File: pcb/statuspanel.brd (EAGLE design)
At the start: 57.1 x 66 mm, 5 parts

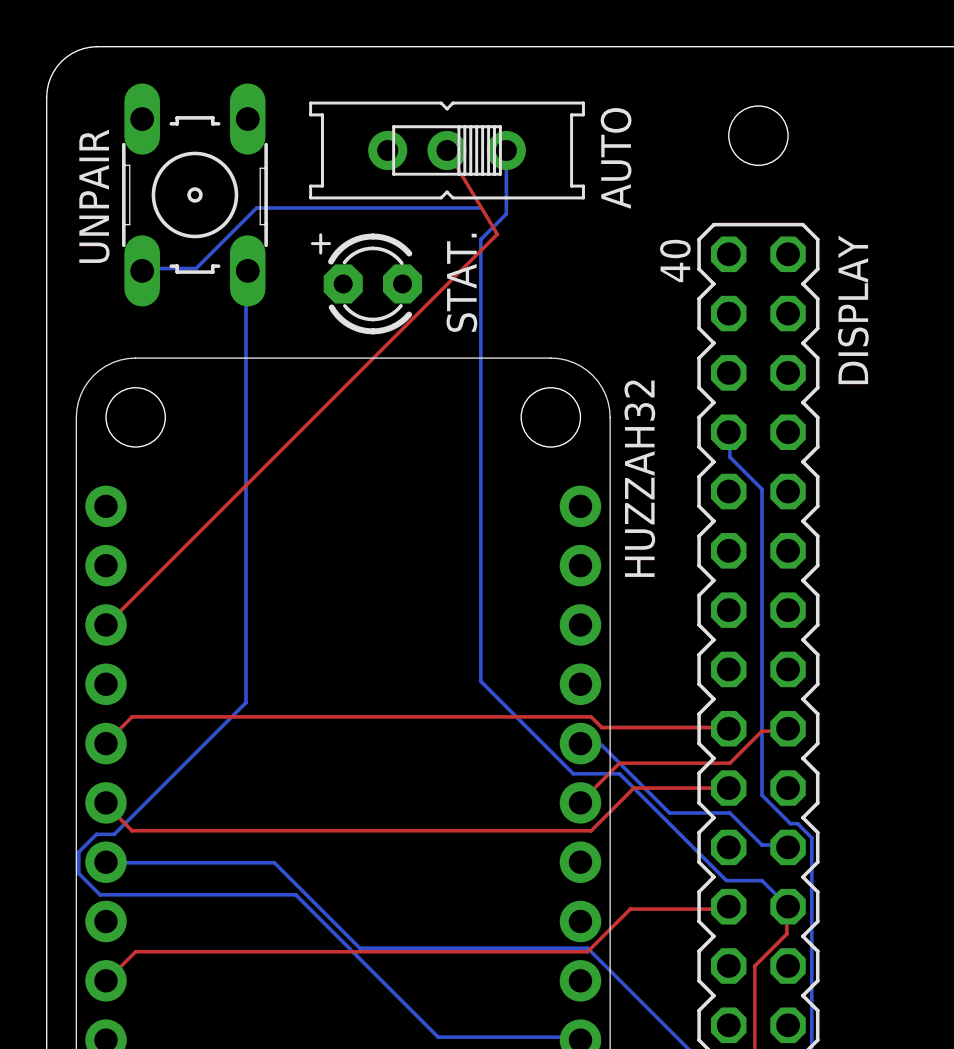
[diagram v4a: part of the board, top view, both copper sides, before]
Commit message: Connect up one leg of the LED
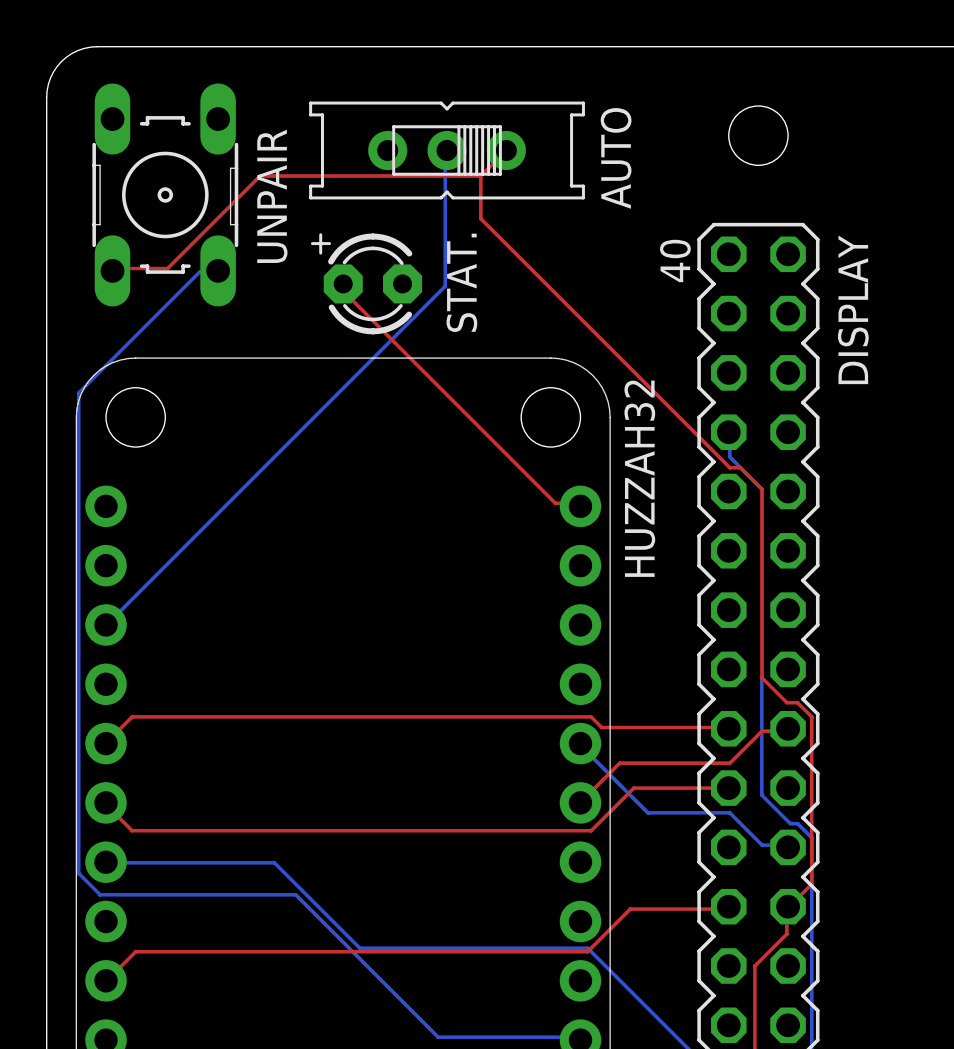
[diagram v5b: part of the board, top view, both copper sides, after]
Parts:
- moved UNPAIR 1.27 mm to (5.08, 59.7)
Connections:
- new net N$3: STAT..K
- new net STATUS: HUZZAH32.16, STAT..A
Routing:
- net STATUS: track 0.00 -> 14.4 mm
- net AUTO: track 27.9 -> 26.4 mm
- net 3V3: track 85.7 -> 86.9 mm
- net UNPAIR: track 53.8 -> 53.2 mm
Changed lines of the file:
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@@
 <attribute name="NAME" x="23.749" y="63.5" size="1.27" layer="25" font="vector" rot="R270"/>
 </element>
-<element name="UNPAIR" library="switch-omron" library_urn="urn:adsk.eagle:library:377" package="B3F-10XX" package3d_urn="urn:adsk.eagle:package:27496/1" value="" x="6.35" y="59.69" smashed="yes" rot="R90">
-<attribute name="MF" value="" x="6.35" y="59.69" size="1.778" layer="27" rot="R90" display="off"/>
-<attribute name="MPN" value="B3F-1000" x="6.35" y="59.69" size="1.778" layer="27" rot="R90" display="off"/>
-<attribute name="NAME" x="2.667" y="56.642" size="1.27" layer="25" ratio="10" rot="R90"/>
-<attribute name="OC_FARNELL" value="176432" x="6.35" y="59.69" size="1.778" layer="27" rot="R90" display="off"/>
-<attribute name="OC_NEWARK" value="36M3542" x="6.35" y="59.69" size="1.778" layer="27" rot="R90" display="off"/>
-<attribute name="POPULARITY" value="72" x="6.35" y="59.69" size="1.778" layer="27" rot="R90" display="off"/>
-<attribute name="VALUE" x="11.43" y="56.642" size="1.27" layer="27" ratio="10" rot="R90"/>
+<element name="UNPAIR" library="switch-omron" library_urn="urn:adsk.eagle:library:377" package="B3F-10XX" package3d_urn="urn:adsk.eagle:package:27496/1" value="" x="5.08" y="59.69" smashed="yes" rot="R90">
+<attribute name="MF" value="" x="5.08" y="59.69" size="1.778" layer="27" rot="R90" display="off"/>
+<attribute name="MPN" value="B3F-1000" x="5.08" y="59.69" size="1.778" layer="27" rot="R90" display="off"/>
+<attribute name="NAME" x="10.287" y="56.642" size="1.27" layer="25" ratio="10" rot="R90"/>
+<attribute name="OC_FARNELL" value="176432" x="5.08" y="59.69" size="1.778" layer="27" rot="R90" display="off"/>
+<attribute name="OC_NEWARK" value="36M3542" x="5.08" y="59.69" size="1.778" layer="27" rot="R90" display="off"/>
+<attribute name="POPULARITY" value="72" x="5.08" y="59.69" size="1.778" layer="27" rot="R90" display="off"/>
+<attribute name="VALUE" x="10.16" y="56.642" size="1.27" layer="27" ratio="10" rot="R90"/>
 </element>
 <element name="STAT." library="adafruit" library_urn="urn:adsk.eagle:library:420" package="LED3MM" package3d_urn="urn:adsk.eagle:package:6240537/1" value="" x="13.97" y="55.88" smashed="yes">
@@
 <wire x1="30.6324" y1="31.8516" x2="31.6992" y2="31.8516" width="0.1524" layer="16"/>
 <wire x1="29.2608" y1="33.2232" x2="30.6324" y2="31.8516" width="0.1524" layer="16"/>
-<wire x1="26.67" y1="33.2232" x2="29.2608" y2="33.2232" width="0.1524" layer="16"/>
-<wire x1="23.7744" y1="36.1188" x2="26.67" y2="33.2232" width="0.1524" layer="16"/>
-<wire x1="22.86" y1="36.1188" x2="23.7744" y2="36.1188" width="0.1524" layer="16"/>
+<wire x1="25.7556" y1="33.2232" x2="29.2608" y2="33.2232" width="0.1524" layer="16"/>
+<wire x1="22.86" y1="36.1188" x2="25.7556" y2="33.2232" width="0.1524" layer="16"/>
 <wire x1="31.6992" y1="31.8516" x2="31.75" y2="31.75" width="0.1524" layer="16"/>
 <wire x1="22.86" y1="36.1188" x2="22.86" y2="36.195" width="0.1524" layer="16"/>
@@
 <contactref element="AUTO" pad="O"/>
 <contactref element="UNPAIR" pad="1"/>
-<wire x1="6.4008" y1="56.5404" x2="4.1148" y2="56.5404" width="0.1524" layer="16"/>
-<wire x1="8.9916" y1="59.1312" x2="6.4008" y2="56.5404" width="0.1524" layer="16"/>
-<wire x1="18.5928" y1="59.1312" x2="8.9916" y2="59.1312" width="0.1524" layer="16"/>
-<wire x1="4.1148" y1="56.5404" x2="4.0894" y2="56.4388" width="0.1524" layer="16"/>
-<wire x1="19.685" y1="61.595" x2="19.685" y2="58.8772" width="0.1524" layer="16"/>
-<wire x1="19.685" y1="58.8772" x2="18.5928" y2="57.785" width="0.1524" layer="16"/>
+<wire x1="5.1816" y1="56.5404" x2="2.8956" y2="56.5404" width="0.1524" layer="1"/>
+<wire x1="9.144" y1="60.5028" x2="5.1816" y2="56.5404" width="0.1524" layer="1"/>
+<wire x1="18.5928" y1="60.5028" x2="9.144" y2="60.5028" width="0.1524" layer="1"/>
+<wire x1="19.685" y1="61.595" x2="18.5928" y2="60.5028" width="0.1524" layer="1"/>
+<wire x1="2.8956" y1="56.5404" x2="2.8194" y2="56.4388" width="0.1524" layer="1"/>
 <wire x1="30.6324" y1="8.9916" x2="31.6992" y2="8.9916" width="0.1524" layer="1"/>
 <wire x1="29.2608" y1="10.3632" x2="29.4132" y2="10.2108" width="0.1524" layer="1"/>
@@
 <wire x1="29.4132" y1="10.2108" x2="30.3276" y2="11.1252" width="0.1524" layer="1"/>
 <wire x1="31.6992" y1="29.1084" x2="31.75" y2="29.21" width="0.1524" layer="1"/>
-<wire x1="18.5928" y1="38.862" x2="18.5928" y2="57.785" width="0.1524" layer="16"/>
-<wire x1="22.5552" y1="34.8996" x2="18.5928" y2="38.862" width="0.1524" layer="16"/>
-<wire x1="24.5364" y1="34.8996" x2="22.5552" y2="34.8996" width="0.1524" layer="16"/>
-<wire x1="29.1084" y1="30.3276" x2="24.5364" y2="34.8996" width="0.1524" layer="16"/>
-<wire x1="30.6324" y1="30.3276" x2="29.1084" y2="30.3276" width="0.1524" layer="16"/>
-<wire x1="31.75" y1="29.21" x2="30.6324" y2="30.3276" width="0.1524" layer="16"/>
+<wire x1="18.5928" y1="58.674" x2="18.5928" y2="60.5028" width="0.1524" layer="1"/>
+<wire x1="29.2608" y1="48.006" x2="18.5928" y2="58.674" width="0.1524" layer="1"/>
+<wire x1="29.718" y1="48.006" x2="29.2608" y2="48.006" width="0.1524" layer="1"/>
+<wire x1="30.6324" y1="47.0916" x2="29.718" y2="48.006" width="0.1524" layer="1"/>
+<wire x1="30.6324" y1="39.0144" x2="30.6324" y2="47.0916" width="0.1524" layer="1"/>
+<wire x1="31.6992" y1="37.9476" x2="30.6324" y2="39.0144" width="0.1524" layer="1"/>
+<wire x1="32.1564" y1="37.9476" x2="31.6992" y2="37.9476" width="0.1524" layer="1"/>
+<wire x1="32.766" y1="37.338" x2="32.1564" y2="37.9476" width="0.1524" layer="1"/>
+<wire x1="32.766" y1="30.1752" x2="32.766" y2="37.338" width="0.1524" layer="1"/>
+<wire x1="31.8516" y1="29.2608" x2="32.766" y2="30.1752" width="0.1524" layer="1"/>
+<wire x1="31.8516" y1="29.2608" x2="31.75" y2="29.21" width="0.1524" layer="1"/>
 </signal>
 <signal name="GND">
@@
 <contactref element="HUZZAH32" pad="19"/>
 <contactref element="AUTO" pad="P"/>
-<wire x1="2.5908" y1="41.3004" x2="19.29765" y2="58.00725" width="0.1524" layer="1"/>
-<wire x1="19.29765" y1="58.00725" x2="17.145" y2="61.595" width="0.1524" layer="1"/>
-<wire x1="2.5908" y1="41.3004" x2="2.54" y2="41.275" width="0.1524" layer="1"/>
+<wire x1="17.0688" y1="55.7784" x2="17.0688" y2="61.5696" width="0.1524" layer="16"/>
+<wire x1="2.5908" y1="41.3004" x2="17.0688" y2="55.7784" width="0.1524" layer="16"/>
+<wire x1="17.0688" y1="61.5696" x2="17.145" y2="61.595" width="0.1524" layer="16"/>
+<wire x1="2.5908" y1="41.3004" x2="2.54" y2="41.275" width="0.1524" layer="16"/>
 </signal>
 <signal name="UNPAIR">
 <contactref element="UNPAIR" pad="3"/>
 <contactref element="HUZZAH32" pad="7"/>
-<wire x1="8.5344" y1="37.9476" x2="8.5344" y2="56.388" width="0.1524" layer="16"/>
-<wire x1="2.8956" y1="32.3088" x2="8.5344" y2="37.9476" width="0.1524" layer="16"/>
-<wire x1="2.1336" y1="32.3088" x2="2.8956" y2="32.3088" width="0.1524" layer="16"/>
-<wire x1="1.3716" y1="31.5468" x2="2.1336" y2="32.3088" width="0.1524" layer="16"/>
-<wire x1="1.3716" y1="30.6324" x2="1.3716" y2="31.5468" width="0.1524" layer="16"/>
+<wire x1="6.5532" y1="56.388" x2="7.3152" y2="56.388" width="0.1524" layer="16"/>
+<wire x1="1.3716" y1="51.2064" x2="6.5532" y2="56.388" width="0.1524" layer="16"/>
+<wire x1="1.3716" y1="30.6324" x2="1.3716" y2="51.2064" width="0.1524" layer="16"/>
 <wire x1="2.286" y1="29.718" x2="1.3716" y2="30.6324" width="0.1524" layer="16"/>
 <wire x1="10.668" y1="29.718" x2="2.286" y2="29.718" width="0.1524" layer="16"/>
 <wire x1="16.764" y1="23.622" x2="10.668" y2="29.718" width="0.1524" layer="16"/>
 <wire x1="22.86" y1="23.622" x2="16.764" y2="23.622" width="0.1524" layer="16"/>
-<wire x1="8.5344" y1="56.388" x2="8.6106" y2="56.4388" width="0.1524" layer="16"/>
+<wire x1="7.3152" y1="56.388" x2="7.3406" y2="56.4388" width="0.1524" layer="16"/>
 <wire x1="22.86" y1="23.622" x2="22.86" y2="23.495" width="0.1524" layer="16"/>
 </signal>
+<signal name="STATUS">
+<contactref element="STAT." pad="A"/>
+<contactref element="HUZZAH32" pad="16"/>
+<wire x1="12.8016" y1="55.4736" x2="12.8016" y2="55.7784" width="0.1524" layer="1"/>
+<wire x1="21.7932" y1="46.482" x2="12.8016" y2="55.4736" width="0.1524" layer="1"/>
+<wire x1="22.86" y1="46.482" x2="21.7932" y2="46.482" width="0.1524" layer="1"/>
+<wire x1="12.8016" y1="55.7784" x2="12.7" y2="55.88" width="0.1524" layer="1"/>
+<wire x1="22.86" y1="46.482" x2="22.86" y2="46.355" width="0.1524" layer="1"/>
+</signal>
+<signal name="N$3">
+<contactref element="STAT." pad="K"/>
+</signal>
 </signals>

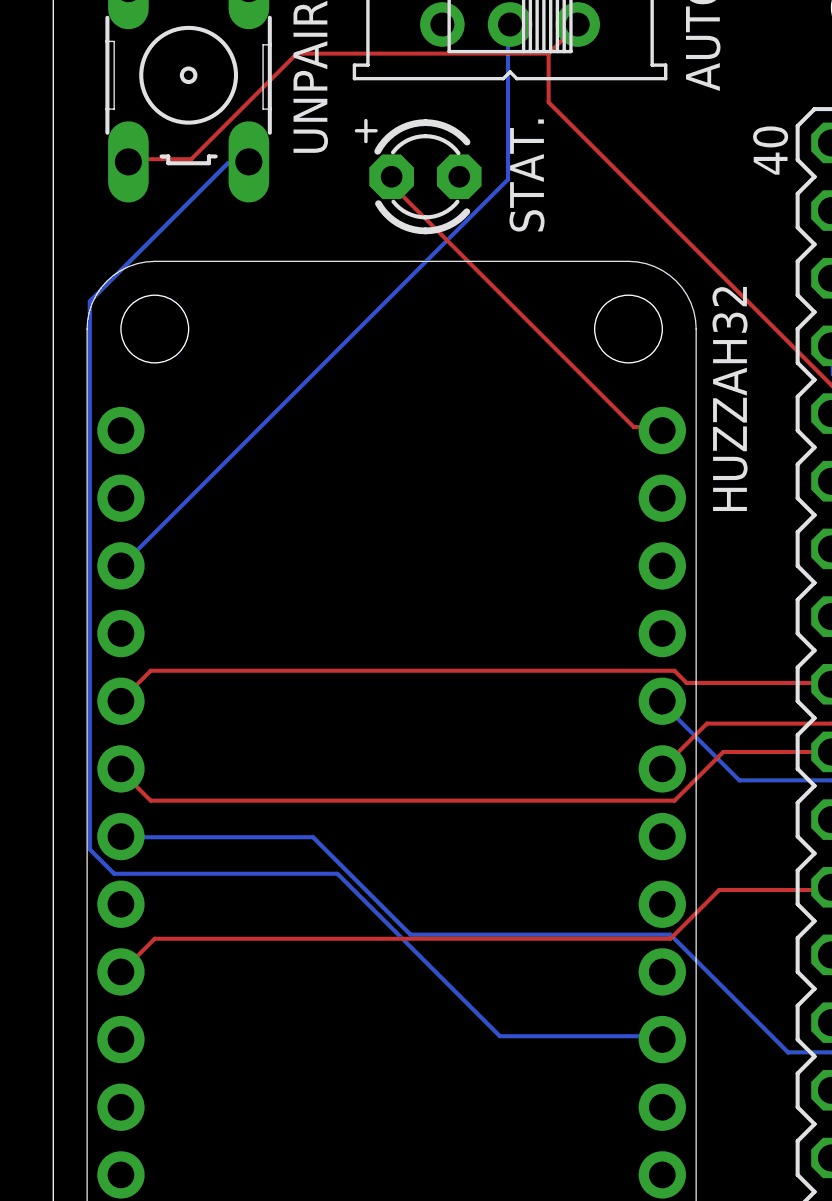
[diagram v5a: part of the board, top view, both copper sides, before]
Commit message: Move un-pair to GPIO 32 / Adafruit-GPIO6.
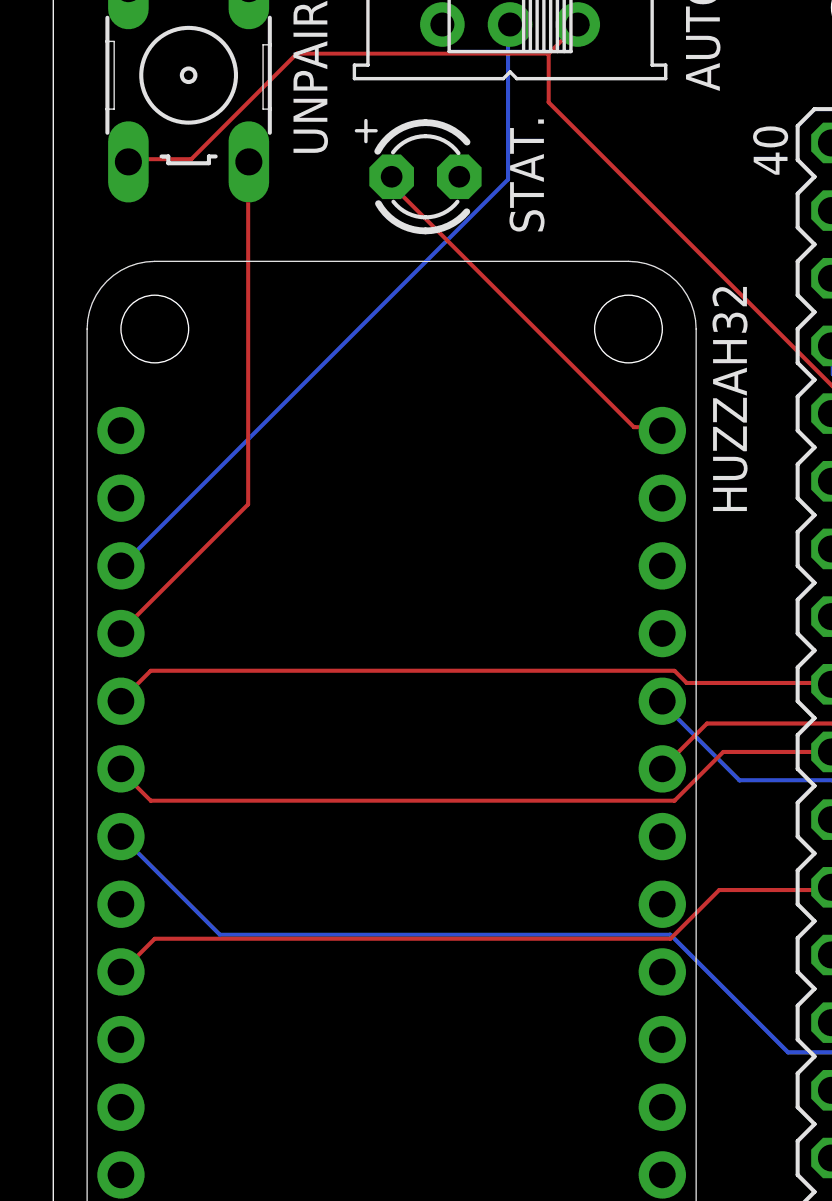
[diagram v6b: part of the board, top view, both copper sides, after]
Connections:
- net UNPAIR: now also HUZZAH32.20; no longer HUZZAH32.7
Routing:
- net UNPAIR: track 53.2 -> 19.7 mm
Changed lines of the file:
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@@
 <wire x1="27.5844" y1="23.0124" x2="29.2608" y2="23.0124" width="0.1524" layer="16"/>
 <wire x1="23.1648" y1="27.432" x2="27.5844" y2="23.0124" width="0.1524" layer="16"/>
-<wire x1="13.4112" y1="27.432" x2="23.1648" y2="27.432" width="0.1524" layer="16"/>
-<wire x1="9.7536" y1="31.0896" x2="13.4112" y2="27.432" width="0.1524" layer="16"/>
-<wire x1="2.5908" y1="31.0896" x2="9.7536" y2="31.0896" width="0.1524" layer="16"/>
+<wire x1="6.2484" y1="27.432" x2="23.1648" y2="27.432" width="0.1524" layer="16"/>
+<wire x1="2.5908" y1="31.0896" x2="6.2484" y2="27.432" width="0.1524" layer="16"/>
 <wire x1="31.6992" y1="21.6408" x2="31.75" y2="21.59" width="0.1524" layer="16"/>
 <wire x1="2.5908" y1="31.0896" x2="2.54" y2="31.115" width="0.1524" layer="16"/>
@@
 <signal name="UNPAIR">
 <contactref element="UNPAIR" pad="3"/>
-<contactref element="HUZZAH32" pad="7"/>
-<wire x1="6.5532" y1="56.388" x2="7.3152" y2="56.388" width="0.1524" layer="16"/>
-<wire x1="1.3716" y1="51.2064" x2="6.5532" y2="56.388" width="0.1524" layer="16"/>
-<wire x1="1.3716" y1="30.6324" x2="1.3716" y2="51.2064" width="0.1524" layer="16"/>
-<wire x1="2.286" y1="29.718" x2="1.3716" y2="30.6324" width="0.1524" layer="16"/>
-<wire x1="10.668" y1="29.718" x2="2.286" y2="29.718" width="0.1524" layer="16"/>
-<wire x1="16.764" y1="23.622" x2="10.668" y2="29.718" width="0.1524" layer="16"/>
-<wire x1="22.86" y1="23.622" x2="16.764" y2="23.622" width="0.1524" layer="16"/>
-<wire x1="7.3152" y1="56.388" x2="7.3406" y2="56.4388" width="0.1524" layer="16"/>
-<wire x1="22.86" y1="23.622" x2="22.86" y2="23.495" width="0.1524" layer="16"/>
+<contactref element="HUZZAH32" pad="20"/>
+<wire x1="7.3152" y1="43.5864" x2="7.3152" y2="56.388" width="0.1524" layer="1"/>
+<wire x1="2.5908" y1="38.862" x2="7.3152" y2="43.5864" width="0.1524" layer="1"/>
+<wire x1="7.3152" y1="56.388" x2="7.3406" y2="56.4388" width="0.1524" layer="1"/>
+<wire x1="2.5908" y1="38.862" x2="2.54" y2="38.735" width="0.1524" layer="1"/>
 </signal>
 <signal name="STATUS">
